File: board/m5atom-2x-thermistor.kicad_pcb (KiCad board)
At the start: 2 copper layers, 20 x 44 mm, 2 parts, among them U1 M5_Atom_3.96Plug, U2 ADS1115IDGS

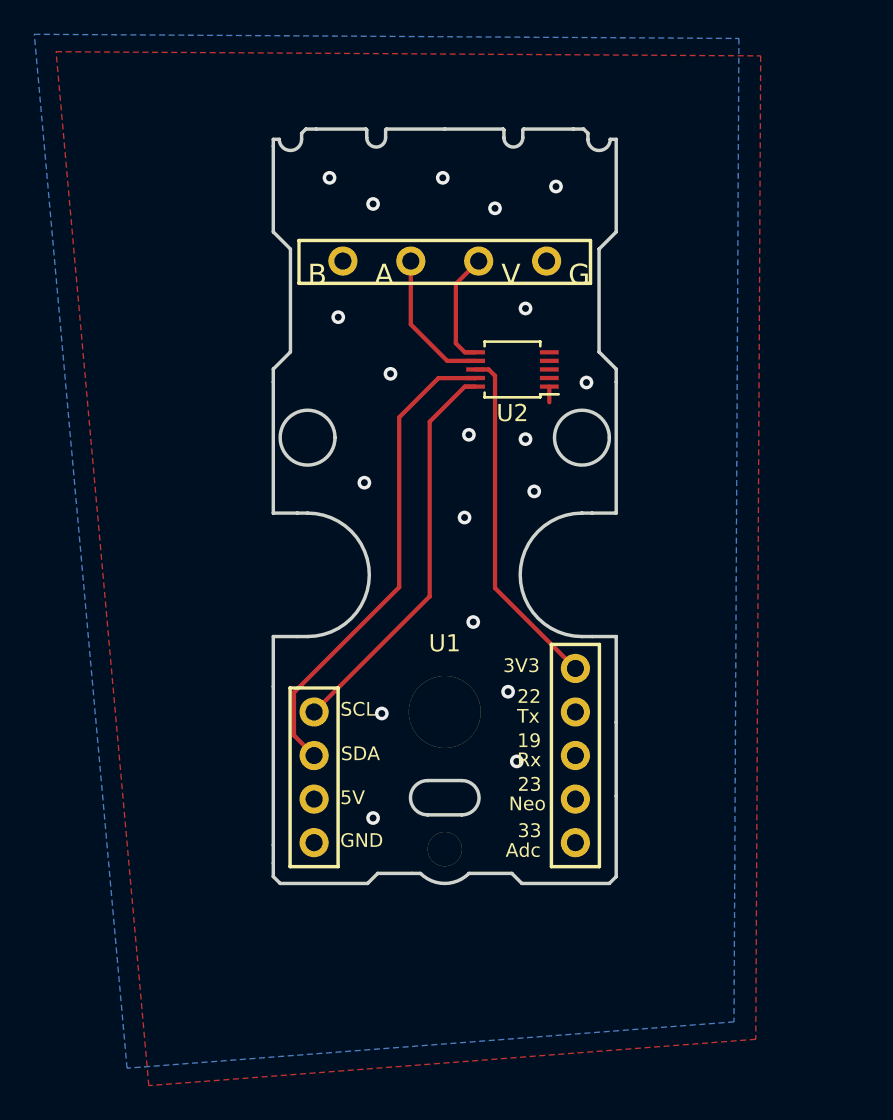
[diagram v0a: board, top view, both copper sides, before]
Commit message: New simple board, introducing mess in submodule...
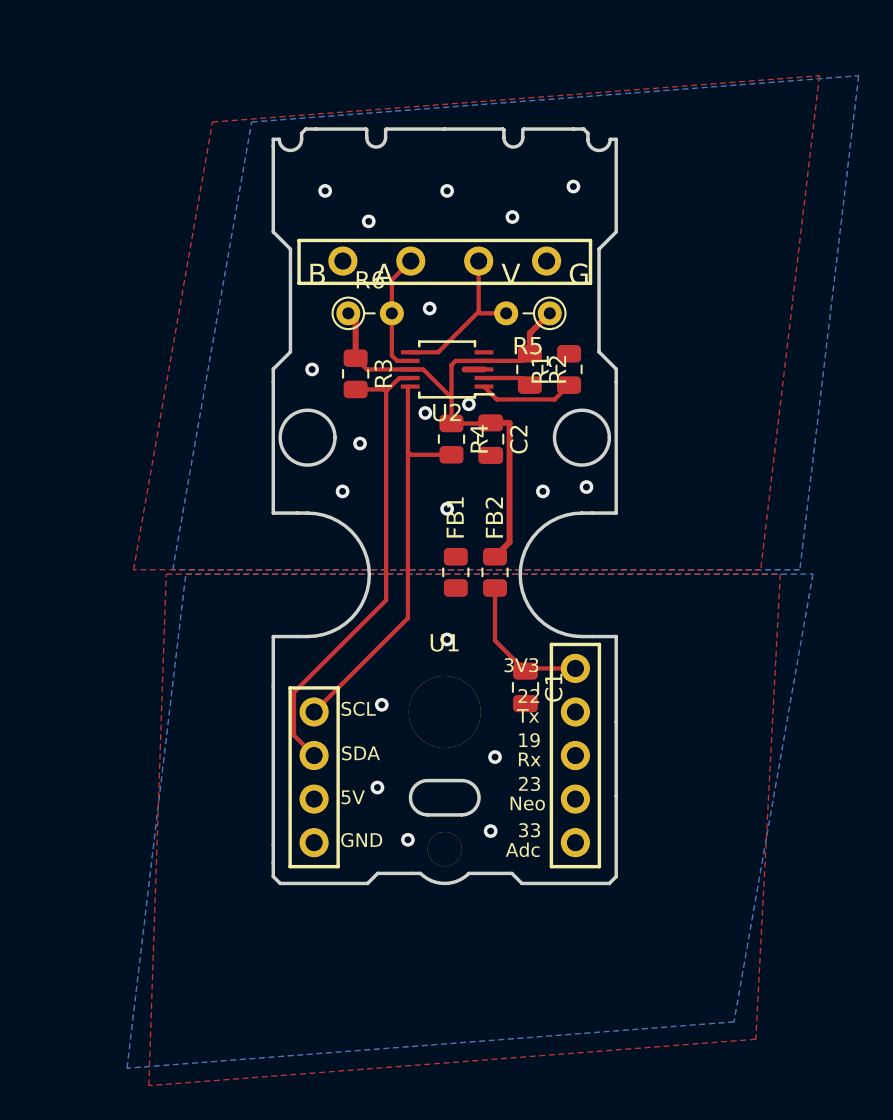
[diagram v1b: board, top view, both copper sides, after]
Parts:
- added C1: 1uF, Capacitor_SMD:C_0805_2012Metric, F.Cu at (124.5, 99.3)
- added C2: 1uF, Capacitor_SMD:C_0805_2012Metric, F.Cu at (122.4, 84.8)
- added FB1: Ferrite_Bead, Resistor_SMD:R_0805_2012Metric, F.Cu at (120.4, 92.6)
- added FB2: Ferrite_Bead, Resistor_SMD:R_0805_2012Metric, F.Cu at (122.7, 92.6)
- added R1: 10k, Resistor_SMD:R_0805_2012Metric, F.Cu at (127.0, 80.8)
- added R2: 10k, Resistor_SMD:R_0805_2012Metric, F.Cu at (124.7, 80.8)
- added R3: 10k, Resistor_SMD:R_0805_2012Metric, F.Cu at (114.6, 81.0)
- added R4: 10k, Resistor_SMD:R_0805_2012Metric, F.Cu at (120.1, 84.8)
- added R5: 200k, Resistor_THT:R_Axial_DIN0204_L3.6mm_D1.6mm_P2.54mm_Vertical, F.Cu at (125.9, 77.5)
- added R6: 200k, Resistor_THT:R_Axial_DIN0204_L3.6mm_D1.6mm_P2.54mm_Vertical, F.Cu at (114.1, 77.5)
- moved U2 3.81 mm to (119.9, 80.8)
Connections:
- U1 pad 10: GND -> GNDA
- U1 pad 13: GND -> GNDA
- U1 pad 5: +3V3 -> Net-(C1-Pad1)
- U2 pad 1: GND -> Net-(R1-Pad1)
- U2 pad 3: Net-(U2-Pad3) -> GNDA
- U2 pad 4: /3V3 -> +3V3
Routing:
- net +3V3: track 20.3 -> 32.0 mm
- net Net-(C1-Pad1): track 0.00 -> 8.56 mm
- net Net-(R1-Pad1): track 0.00 -> 5.62 mm
- net Net-(R5-Pad2): track 6.72 -> 9.57 mm
- net Net-(R2-Pad2): track 0.00 -> 2.85 mm
- net Net-(R6-Pad2): track 8.35 -> 7.17 mm
- net GNDA: track 0.00 -> 1.13 mm, vias 0 -> 14
- net GND: track 0.91 -> 0.00 mm, vias 19 -> 6
- net /SDA: track 28.2 -> 27.5 mm
- net /CLK: track 23.2 -> 23.9 mm
- added copper zone on B.Cu, net GNDA
- added copper zone on F.Cu, net GNDA
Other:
- net class Supply added: clearance 0.2, trace_width 0.35, via_dia 0.8, via_drill 0.4
